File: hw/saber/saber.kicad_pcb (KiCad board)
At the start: 4 copper layers, 60.7 x 27.2 mm, 73 parts, among them J1 282834-2, J2 282834-2, J3 OSTVN12A150, J4 NUCLEO144ZE-STLINK, Q1 STL120N4F6AG, Q2 SIS413DN-T1-GE3, Q3 SSM3K337R, Q4 STL76DN4LF7AG, Q5 SSM3K337R, Q6 SSM3K337R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

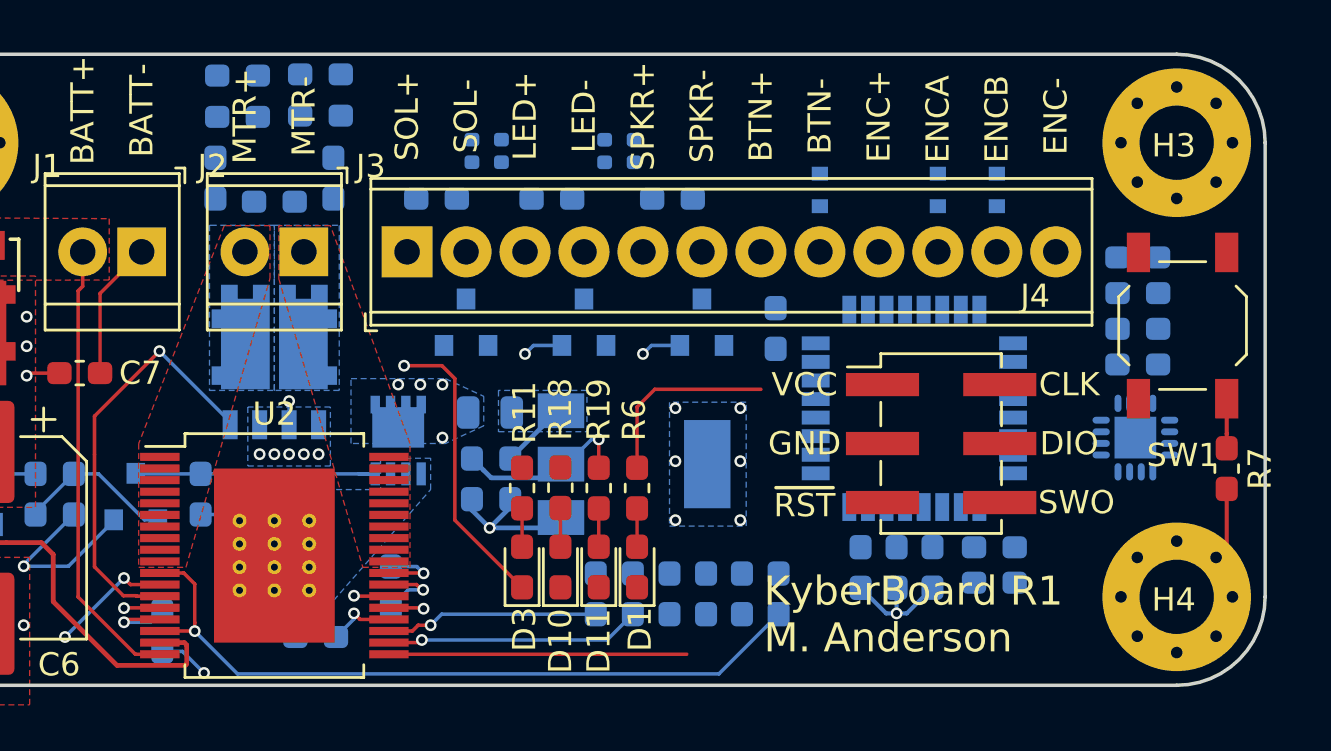
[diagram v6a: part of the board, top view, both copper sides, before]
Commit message: noted more pin-specific capacitor connections
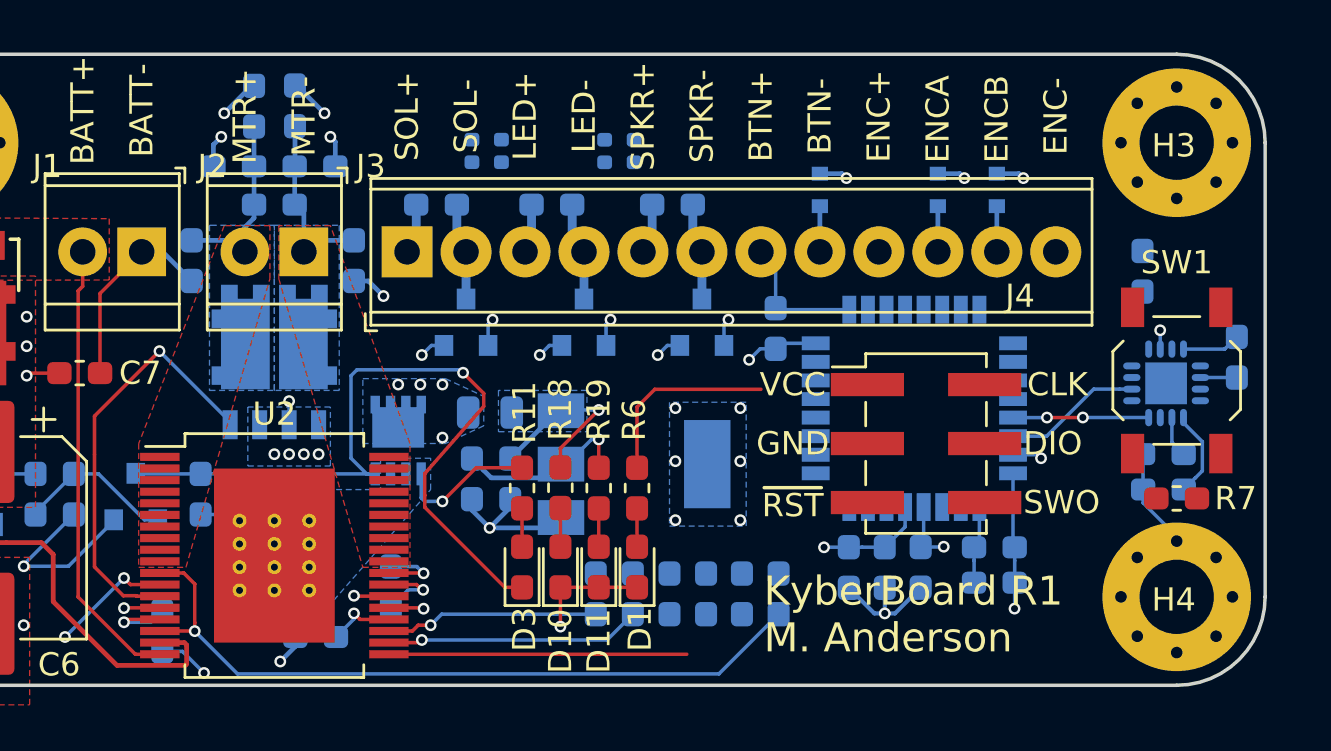
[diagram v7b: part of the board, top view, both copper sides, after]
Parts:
- moved C17 8.54 mm to (172.7, 80.5)
- moved C15 7.01 mm to (172.7, 82.0)
- moved D5 5.14 mm to (136.1, 68.1), turned to 180 degrees
- moved C16 5.08 mm to (175.8, 76.3), turned to 270 degrees
- moved R20 4.02 mm to (171.8, 72.6), turned to 90 degrees
- moved C10 3.70 mm to (130.8, 72.1), turned to 270 degrees
- moved C11 3.67 mm to (137.8, 72.1), turned to 270 degrees
- moved D6 3.17 mm to (133.5, 65.5), turned to 90 degrees
- moved U4 2.68 mm to (172.8, 77.4)
- moved R7 2.51 mm to (173.2, 82.4), turned to 180 degrees
- moved SW1 2.38 mm to (173.2, 77.3)
- moved D4 2.14 mm to (132.6, 68.1)
- moved D7 1.17 mm to (135.3, 65.5), turned to 90 degrees
- moved J4 0.65 mm to (162.4, 80.0)
- moved C19 0.51 mm to (160.7, 85.4)
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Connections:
- D4 pad 1: /BATT+ -> /hbridge/VCC
- D5 pad 1: /BATT+ -> /hbridge/VCC
- R18 pad 1: +12V -> +12C
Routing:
- net GND: track 42.5 -> 83.2 mm, vias 17 -> 29
- net +3V3: track 13.0 -> 35.3 mm, vias 9 -> 11
- net Net-(D3-Pad1): track 24.0 -> 33.3 mm
- net /hbridge/VCC: track 2.69 -> 11.5 mm, vias 3 -> 6
- net /MOT+: track 0.00 -> 8.20 mm
- net /MOT-: track 0.00 -> 7.94 mm
- net /acc/SDA: track 0.00 -> 5.96 mm
- net /acc/SCL: track 0.00 -> 5.85 mm, vias 0 -> 2
- net +12C: track 3.04 -> 7.84 mm, vias 0 -> 1
- net /SPKR-: track 0.56 -> 4.28 mm
- net /SOL-: track 0.56 -> 4.23 mm
- net /LED-: track 0.72 -> 4.27 mm
- net Net-(R7-Pad1): track 2.14 -> 0.00 mm
- net /ENC_B: track 1.02 -> 2.98 mm
- net /ENC_A: track 0.00 -> 1.97 mm
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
